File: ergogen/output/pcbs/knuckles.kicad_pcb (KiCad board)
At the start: 2 copper layers, 130.3 x 107.9 mm, 120 parts

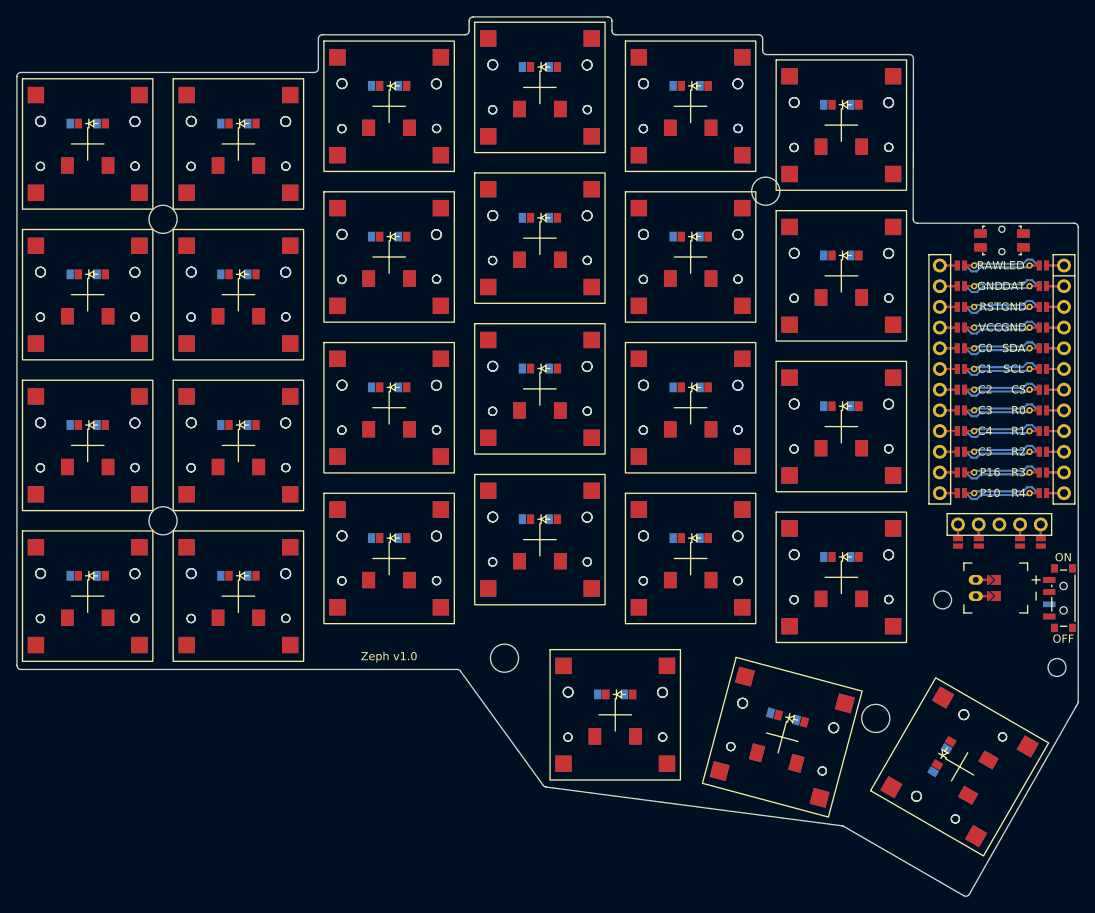
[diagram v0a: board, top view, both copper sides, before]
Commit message: feat: renamed zeph board to knuckles (#1)
* feat: renamed zeph

* fix: github action board name

* chore: more renaming
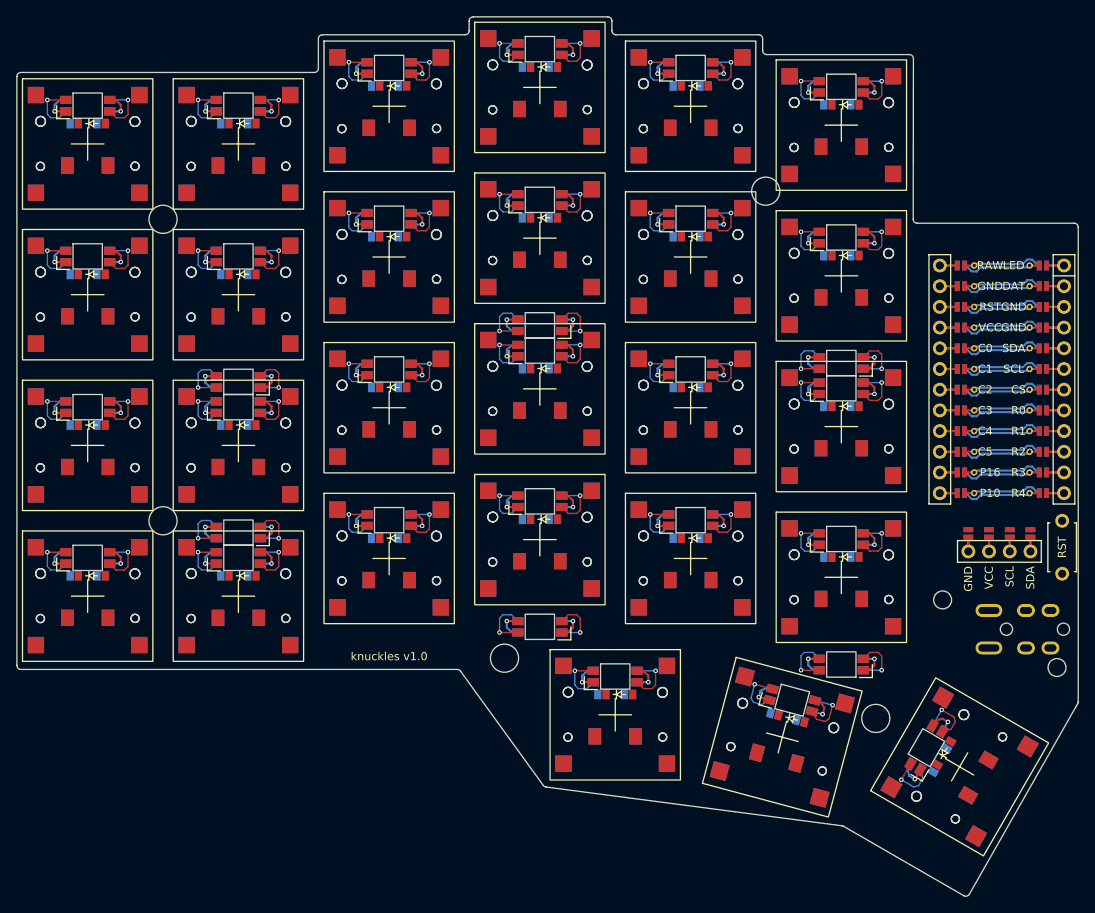
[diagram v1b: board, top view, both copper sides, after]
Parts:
- removed JST1: , ceoloide:battery_connector_jst_ph_2
- removed PWR1: , ceoloide:power_switch_smd_side
- added LED1: , ceoloide:led_SK6812mini-e (per-key, reversible), B.Cu at (100.0, 95.3)
- added LED10: , ceoloide:led_SK6812mini-e (per-key, reversible), B.Cu at (137.0, 72.2)
- added LED11: , ceoloide:led_SK6812mini-e (per-key, reversible), B.Cu at (137.0, 53.7)
- added LED12: , ceoloide:led_SK6812mini-e (per-key, reversible), B.Cu at (137.0, 35.2)
- added LED13: , ceoloide:led_SK6812mini-e (per-key, reversible), B.Cu at (155.5, 88.4)
- added LED14: , ceoloide:led_SK6812mini-e (per-key, reversible), B.Cu at (155.5, 69.9)
- added LED15: , ceoloide:led_SK6812mini-e (per-key, reversible), B.Cu at (155.5, 51.4)
- added LED16: , ceoloide:led_SK6812mini-e (per-key, reversible), B.Cu at (155.5, 32.9)
- added LED17: , ceoloide:led_SK6812mini-e (per-key, reversible), B.Cu at (174.0, 90.7)
- added LED18: , ceoloide:led_SK6812mini-e (per-key, reversible), B.Cu at (174.0, 72.2)
- added LED19: , ceoloide:led_SK6812mini-e (per-key, reversible), B.Cu at (174.0, 53.7)
- added LED2: , ceoloide:led_SK6812mini-e (per-key, reversible), B.Cu at (100.0, 76.8)
- added LED20: , ceoloide:led_SK6812mini-e (per-key, reversible), B.Cu at (174.0, 35.2)
- added LED21: , ceoloide:led_SK6812mini-e (per-key, reversible), B.Cu at (192.5, 93.0)
- added LED22: , ceoloide:led_SK6812mini-e (per-key, reversible), B.Cu at (192.5, 74.5)
- added LED23: , ceoloide:led_SK6812mini-e (per-key, reversible), B.Cu at (192.5, 56.0)
- added LED24: , ceoloide:led_SK6812mini-e (per-key, reversible), B.Cu at (192.5, 37.5)
- added LED25: , ceoloide:led_SK6812mini-e (per-key, reversible), B.Cu at (164.8, 109.9)
- added LED26: , ceoloide:led_SK6812mini-e (per-key, reversible), B.Cu at (186.5, 112.8)
- added LED27: , ceoloide:led_SK6812mini-e (per-key, reversible), B.Cu at (202.9, 118.6)
- added LED28: , ceoloide:led_SK6812mini-e (underglow, reversible), B.Cu at (192.5, 71.4)
- added LED29: , ceoloide:led_SK6812mini-e (underglow, reversible), B.Cu at (155.5, 66.8)
- added LED3: , ceoloide:led_SK6812mini-e (per-key, reversible), B.Cu at (100.0, 58.3)
- added LED30: , ceoloide:led_SK6812mini-e (underglow, reversible), B.Cu at (118.5, 73.7)
- added LED31: , ceoloide:led_SK6812mini-e (underglow, reversible), B.Cu at (118.5, 92.2)
- added LED32: , ceoloide:led_SK6812mini-e (underglow, reversible), B.Cu at (155.5, 103.8)
- added LED33: , ceoloide:led_SK6812mini-e (underglow, reversible), B.Cu at (192.5, 108.4)
- added LED4: , ceoloide:led_SK6812mini-e (per-key, reversible), B.Cu at (100.0, 39.8)
- added LED5: , ceoloide:led_SK6812mini-e (per-key, reversible), B.Cu at (118.5, 95.3)
- added LED6: , ceoloide:led_SK6812mini-e (per-key, reversible), B.Cu at (118.5, 76.8)
- added LED7: , ceoloide:led_SK6812mini-e (per-key, reversible), B.Cu at (118.5, 58.3)
- added LED8: , ceoloide:led_SK6812mini-e (per-key, reversible), B.Cu at (118.5, 39.8)
- added LED9: , ceoloide:led_SK6812mini-e (per-key, reversible), B.Cu at (137.0, 90.7)
- added TRRS1: , ceoloide:trrs_pj320a (reversible, symmetric), F.Cu at (221.4, 104.1)
- DISP1: footprint ceoloide:display_nice_view -> ceoloide:display_ssd1306
- RST1: footprint ceoloide:reset_switch_smd_side -> ceoloide:reset_switch_tht_top
- moved RST1 38.4 mm to (219.6, 94.0), turned to 90 degrees
- moved DISP1 3.31 mm to (211.9, 77.8)
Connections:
- DISP1 pad 10: CS -> DISP1_4
- DISP1 pad 11: GND -> DISP1_3
- DISP1 pad 12: SCL -> DISP1_2
- DISP1 pad 13: SDA -> DISP1_1
- DISP1 pad 14: DISP1_1 -> GND
- DISP1 pad 15: DISP1_2 -> VCC
- DISP1 pad 16: DISP1_4 -> SCL
- DISP1 pad 17: DISP1_5 -> SDA
- DISP1 pad 20: CS -> DISP1_1
- DISP1 pad 21: GND -> DISP1_2
- DISP1 pad 22: SCL -> DISP1_3
- DISP1 pad 23: SDA -> DISP1_4
- DISP1 pad 24: DISP1_5 -> GND
- DISP1 pad 25: DISP1_4 -> VCC
- DISP1 pad 26: DISP1_2 -> SCL
- DISP1 pad 27: DISP1_1 -> SDA
- DISP1 pad 3: VCC -> DISP1_3
- RST1 pad 1: GND -> RST
- RST1 pad 2: RST -> GND
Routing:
- net VCC: track 0.00 -> 127.4 mm, vias 0 -> 33
- net GND: track 3.50 -> 127.4 mm, vias 0 -> 33
- net (no net): track 333.1 -> 414.2 mm, vias 0 -> 12
- net ULED_5: track 0.00 -> 13.5 mm, vias 0 -> 2
- net ULED_4: track 0.00 -> 13.5 mm, vias 0 -> 2
- net ULED_3: track 0.00 -> 13.5 mm, vias 0 -> 2
- net ULED_2: track 0.00 -> 13.5 mm, vias 0 -> 2
- net ULED_1: track 0.00 -> 13.5 mm, vias 0 -> 2
- net LED_9: track 0.00 -> 13.5 mm, vias 0 -> 2
- net LED_6: track 0.00 -> 13.5 mm, vias 0 -> 2
- net LED_5: track 0.00 -> 13.5 mm, vias 0 -> 2
- net LED_4: track 0.00 -> 13.5 mm, vias 0 -> 2
- net LED_3: track 0.00 -> 13.5 mm, vias 0 -> 2
- net LED_20: track 0.00 -> 13.5 mm, vias 0 -> 2
- net LED_2: track 0.00 -> 13.5 mm, vias 0 -> 2
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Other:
- board text added: "knuckles v1.0"
- board text removed: "Zeph v1.0"
